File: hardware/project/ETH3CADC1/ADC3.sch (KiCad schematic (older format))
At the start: 45 parts, among them U801 DG211B, U802 OPA2192, U803 DG419xY, U804 LT5400-100k-100k, U805 LT5400-5k-1k, U806 OPA177, U807 OPA140, U808 OPA192, U809 LT5400-10k-10k, U810 LM311

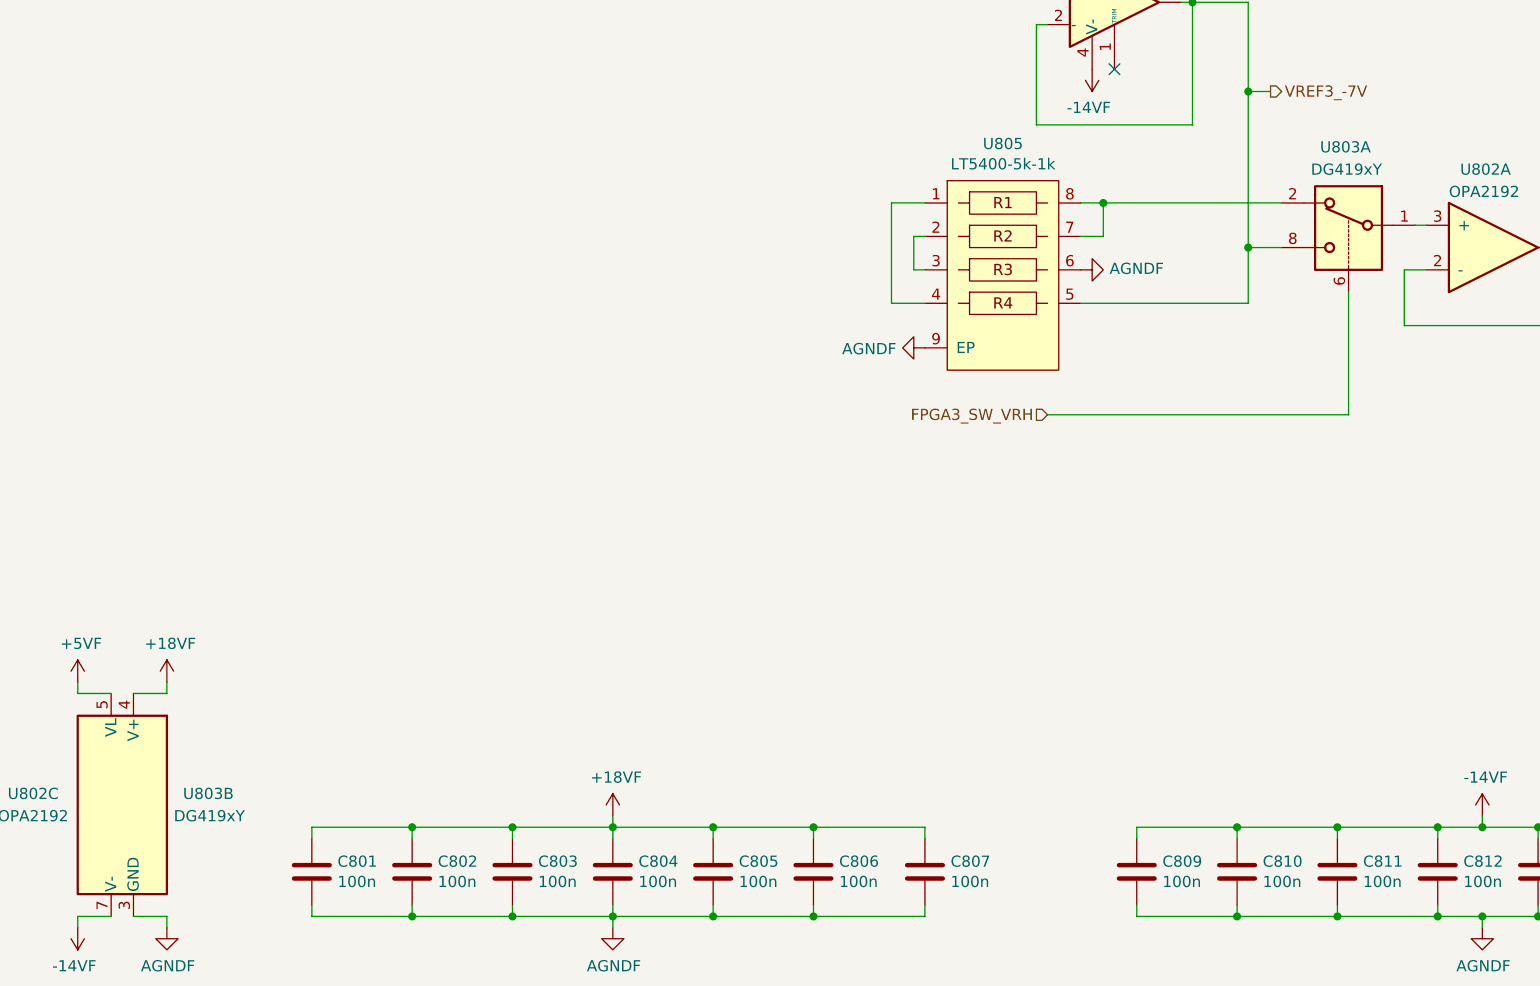
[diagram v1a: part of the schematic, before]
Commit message: Fixed mistake with DG419. Never use DG419Lxx variant.
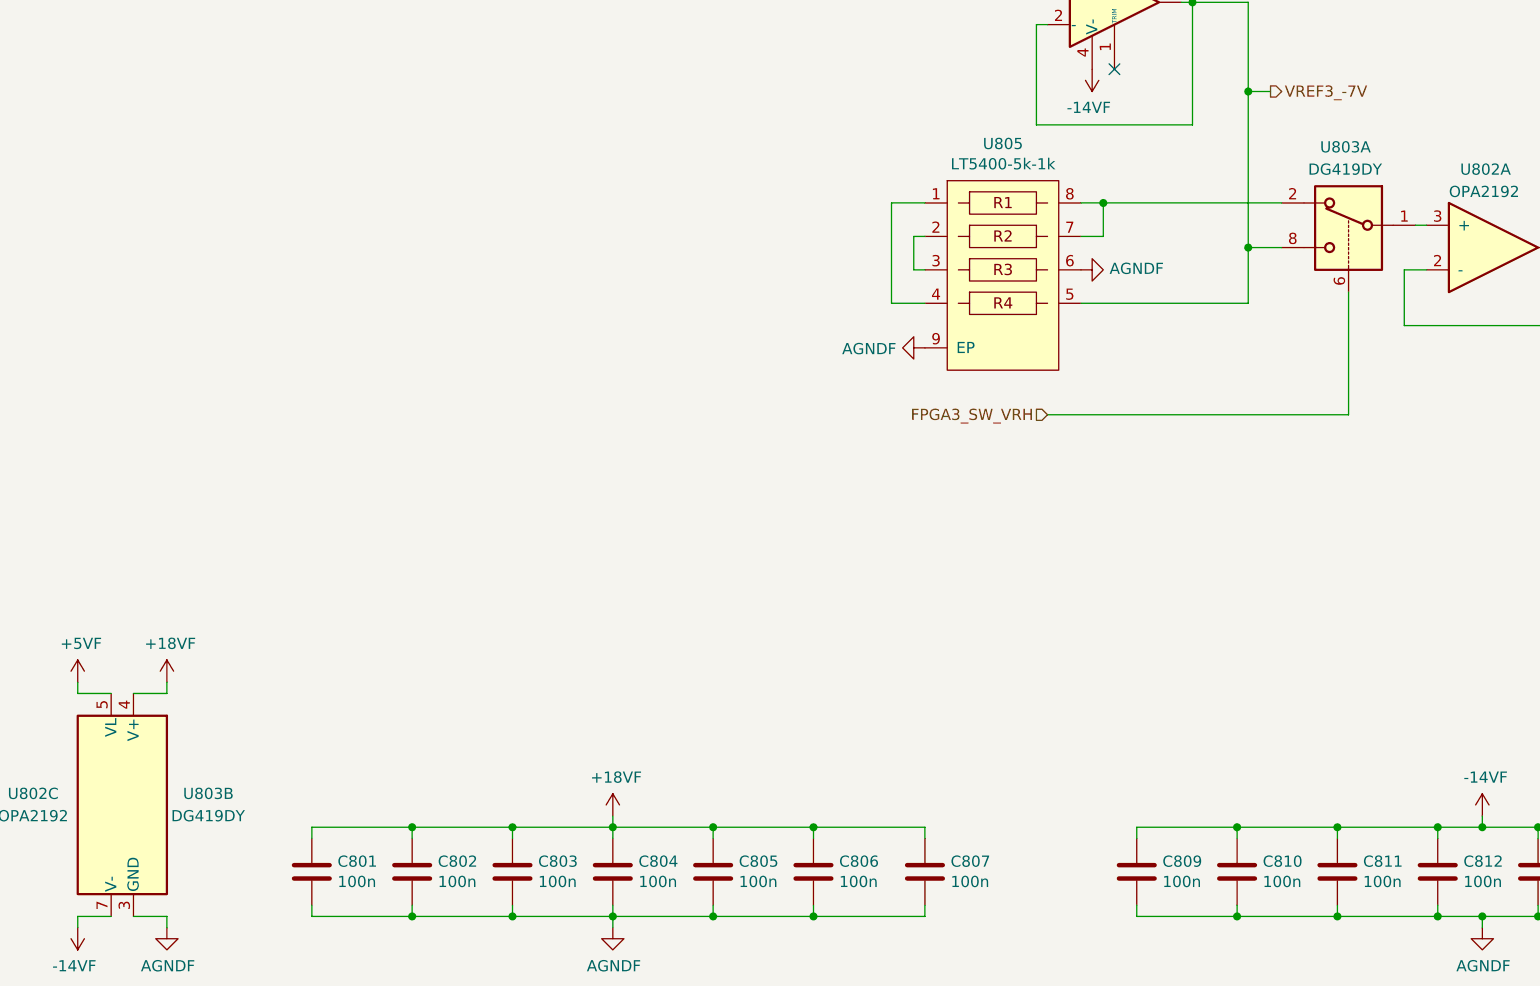
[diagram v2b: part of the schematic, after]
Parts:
- U803: value DG419xY -> DG419DY
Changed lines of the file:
@@
 AR Path="/605B3009/605E7BBD" Ref="U803"  Part="1"
 F 0 "U803" H 7950 7850 50  0000 L CNN
-F 1 "DG419xY" H 7900 7750 50  0000 L CNN
+F 1 "DG419DY" H 7900 7750 50  0000 L CNN
 F 2 "Package_SO:SOIC-8_3.9x4.9mm_P1.27mm" H 8050 7300 50  0001 C CNN
 F 3 "https://datasheets.maximintegrated.com/en/ds/DG417-DG419.pdf" H 8050 7600 50  0001 C CNN
@@
 AR Path="/605B3009/605E7C4B" Ref="U803"  Part="2"
 F 0 "U803" H 2150 10350 50  0000 L CNN
-F 1 "DG419xY" H 2100 10250 50  0000 L CNN
+F 1 "DG419DY" H 2100 10250 50  0000 L CNN
 F 2 "Package_SO:SOIC-8_3.9x4.9mm_P1.27mm" H 2600 10000 50  0001 C CNN
 F 3 "https://datasheets.maximintegrated.com/en/ds/DG417-DG419.pdf" H 2600 10300 50  0001 C CNN

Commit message: Development
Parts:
- removed C801, C802, C803, C804, C805, C806, C807, C809, C810, C811, C812, C814, C816, C817, C818, C819, C820, C821: 100n, Capacitor_SMD:C_0402_1005Metric_Pad0.74x0.62mm_HandSolder, symbol Device:C
- removed C808: 2n2/SMD, Capacitor_SMD:C_0603_1608Metric_Pad1.08x0.95mm_HandSolder, symbol Device:C
- removed C813: 33p, Capacitor_SMD:C_0402_1005Metric_Pad0.74x0.62mm_HandSolder, symbol Device:C
- removed C815: DNP, Capacitor_SMD:C_0402_1005Metric_Pad0.74x0.62mm_HandSolder, symbol Device:C
- removed D801, D802: BAV21W, Diode_SMD:D_SOD-123, symbol Device:D
- removed R801, R802, R804, R805, R809: 10, Resistor_SMD:R_0402_1005Metric_Pad0.72x0.64mm_HandSolder, symbol Device:R
- removed R803: 12k/.05%, Resistor_SMD:R_0603_1608Metric_Pad0.98x0.95mm_HandSolder, symbol Device:R
- removed R806: 62k, Resistor_SMD:R_0402_1005Metric_Pad0.72x0.64mm_HandSolder, symbol Device:R
- removed R807: 620/.05%, Resistor_SMD:R_0603_1608Metric_Pad0.98x0.95mm_HandSolder, symbol Device:R
- removed R808, R812: 3k9/.05%, Resistor_SMD:R_0603_1608Metric_Pad0.98x0.95mm_HandSolder, symbol Device:R
- removed R810: 62/.1%, Resistor_SMD:R_0603_1608Metric_Pad0.98x0.95mm_HandSolder, symbol Device:R
- removed R811: 39k/.05%, Resistor_SMD:R_0603_1608Metric_Pad0.98x0.95mm_HandSolder, symbol Device:R
- removed U801: DG211B, Package_SO:TSSOP-16_4.4x5mm_P0.65mm, symbol ETH3CDAQ1:DG211
- removed U802: OPA2192, Package_SO:SOIC-8_3.9x4.9mm_P1.27mm, symbol ETH3CDAQ1:OPA2192
- removed U803: DG419DY, Package_SO:SOIC-8_3.9x4.9mm_P1.27mm, symbol Analog_Switch:DG419xY
- removed U804: LT5400-100k-100k, Package_SO:MSOP-8-1EP_3x3mm_P0.65mm_EP1.73x1.85mm_ThermalVias, symbol ETH3CDAQ1:LT5400-100k-100k
- removed U805: LT5400-5k-1k, Package_SO:MSOP-8-1EP_3x3mm_P0.65mm_EP1.73x1.85mm_ThermalVias, symbol ETH3CDAQ1:LT5400-5k-1k
- removed U806: OPA177, Package_SO:SOIC-8_3.9x4.9mm_P1.27mm, symbol ETH3CDAQ1:OPA177
- removed U807: OPA140, Package_SO:SOIC-8_3.9x4.9mm_P1.27mm, symbol ETH3CDAQ1:OPA140
- removed U808: OPA192, Package_SO:SOIC-8_3.9x4.9mm_P1.27mm, symbol ETH3CDAQ1:OPA192
- removed U809: LT5400-10k-10k, Package_SO:MSOP-8-1EP_3x3mm_P0.65mm_EP1.73x1.85mm_ThermalVias, symbol ETH3CDAQ1:LT5400-10k-10k
- removed U810: LM311, Package_SO:SOIC-8_3.9x4.9mm_P1.27mm, symbol Comparator:LM311
- added C1701, C1702, C1703, C1704, C1705, C1706, C1707, C1708, C1709, C1711, C1712, C1713, C1714, C1715, C1717, C1718, C1719, C1720, C1721: 100n, Capacitor_SMD:C_0402_1005Metric_Pad0.74x0.62mm_HandSolder, symbol Device:C
- added C1710: 2n2/SMD, Capacitor_SMD:C_0603_1608Metric_Pad1.08x0.95mm_HandSolder, symbol Device:C
- added C1716: 33p, Capacitor_SMD:C_0402_1005Metric_Pad0.74x0.62mm_HandSolder, symbol Device:C
- added D1701, D1702: BAV21W, Diode_SMD:D_SOD-123, symbol Device:D
- added R1701, R1702, R1703, R1704, R1707: 10k, Resistor_SMD:R_0402_1005Metric_Pad0.72x0.64mm_HandSolder, symbol Device:R
- added R1705: 10M, Resistor_SMD:R_0603_1608Metric_Pad0.98x0.95mm_HandSolder, symbol Device:R
- added R1706: 0, Resistor_SMD:R_0402_1005Metric_Pad0.72x0.64mm_HandSolder, symbol Device:R
- added R1708, R1718: 62/.1%, Resistor_SMD:R_0603_1608Metric_Pad0.98x0.95mm_HandSolder, symbol Device:R
- added R1709, R1710, R1712, R1713, R1717: 10, Resistor_SMD:R_0402_1005Metric_Pad0.72x0.64mm_HandSolder, symbol Device:R
- added R1711: 12k/.05%, Resistor_SMD:R_0603_1608Metric_Pad0.98x0.95mm_HandSolder, symbol Device:R
- added R1714: 62k, Resistor_SMD:R_0402_1005Metric_Pad0.72x0.64mm_HandSolder, symbol Device:R
- added R1715: 620/.05%, Resistor_SMD:R_0603_1608Metric_Pad0.98x0.95mm_HandSolder, symbol Device:R
- added R1716, R1720: 3k9/.05%, Resistor_SMD:R_0603_1608Metric_Pad0.98x0.95mm_HandSolder, symbol Device:R
- added R1719: 39k/.05%, Resistor_SMD:R_0603_1608Metric_Pad0.98x0.95mm_HandSolder, symbol Device:R
- added U1701, U1703: DG211, Package_SO:TSSOP-16_4.4x5mm_P0.65mm, symbol ETH3CDAQ1:DG211
- added U1702: DG211B, Package_SO:TSSOP-16_4.4x5mm_P0.65mm, symbol ETH3CDAQ1:DG211
- added U1704: OPA2192, Package_SO:SOIC-8_3.9x4.9mm_P1.27mm, symbol ETH3CDAQ1:OPA2192
- added U1705: DG419DY, Package_SO:SOIC-8_3.9x4.9mm_P1.27mm, symbol Analog_Switch:DG419xY
- added U1706, U1710: OPA140, Package_SO:SOIC-8_3.9x4.9mm_P1.27mm, symbol ETH3CDAQ1:OPA140
- added U1707: LT5400-100k-100k, Package_SO:MSOP-8-1EP_3x3mm_P0.65mm_EP1.73x1.85mm_ThermalVias, symbol ETH3CDAQ1:LT5400-100k-100k
- added U1708: LT5400-5k-1k, Package_SO:MSOP-8-1EP_3x3mm_P0.65mm_EP1.73x1.85mm_ThermalVias, symbol ETH3CDAQ1:LT5400-5k-1k
- added U1709: OPA177, Package_SO:SOIC-8_3.9x4.9mm_P1.27mm, symbol ETH3CDAQ1:OPA177
- added U1711: LT5400-10k-10k, Package_SO:MSOP-8-1EP_3x3mm_P0.65mm_EP1.73x1.85mm_ThermalVias, symbol ETH3CDAQ1:LT5400-10k-10k
- added U1712: OPA192, Package_SO:SOIC-8_3.9x4.9mm_P1.27mm, symbol ETH3CDAQ1:OPA192
- added U1713: LM311, Package_SO:SOIC-8_3.9x4.9mm_P1.27mm, symbol Comparator:LM311
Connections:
- net +18VF: now also C1701.1, C1702.1, C1703.1, C1705.1, C1706.1, C1707.1, C1708.1, R1709.1, R1712.1, U1701.13 (V+), U1702.13 (V+), U1704.4 (V-), U1705.4 (V+), U1706.7 (V+), U1709.7 (V+)
- net -14VF: now also C1709.1, C1711.1, C1712.1, C1713.1, C1714.1, C1715.1, C1717.1, C1718.1, R1710.2, R1713.2, R1717.2, U1701.4 (V-), U1702.4 (V-), U1704.8 (V+), U1705.7 (V-), U1706.4 (V-), U1709.4 (V-)
- net ADIN3: now also R1701.2
- net AD_COMP3: now also R1720.2, U1713.7
- net AGNDF: now also C1701.2, C1702.2, C1703.2, C1704.2, C1705.2, C1706.2, C1707.2, C1708.2, C1709.2, C1711.2, C1712.2, C1713.2, C1714.2, C1715.2, C1717.2, C1718.2, R1702.2, R1705.2, R1715.2, U1701.5 (GND), U1702.5 (GND), U1704.6 (-), U1705.3 (GND), U1707.9 (EP), U1708.6, U1708.9 (EP), U1710.3 (+), U1711.9 (EP), U1712.3 (+)
- net DGNDF: now also C1719.2, C1720.2, U1713.1 (GND)
- net FGPA3_AD_ID: now also U1702.16
- net FGPA3_AD_IIN: now also U1702.1
- net FGPA3_AD_IRN: now also U1702.8
- net FGPA3_AD_IRP: now also U1702.9
- net FPGA3_SW_VRH: now also U1705.6
- net VREF+: now also U1704.7, U1707.4, U1711.1, U1711.2
- net VREF-: now also U1704.1, U1704.2 (-), U1707.3, U1711.3, U1711.4
- net VREF_N7V_LPF: now also R1704.2, R1708.2
- new net: U1707.1, U1707.2
- new net: U1702.6, U1707.5
- new net: U1702.11, U1707.6
- new net: U1702.2, U1707.7
- new net: R1707.1, U1707.8
- new net: C1710.2, U1702.10, U1702.14, U1702.3, U1702.7, U1710.2 (-)
- new net: U1704.5 (+), U1711.5, U1711.6, U1711.7, U1711.8
- new net: C1710.1, R1711.2, U1702.15, U1710.6
- new net: U1704.3 (+), U1705.1
- new net: U1705.2, U1708.7, U1708.8
- new net: U1705.8, U1708.5, U1709.2 (-), U1709.6
- new net: R1706.1, R1707.2, U1706.2 (-), U1706.6
- new net: R1705.1, R1706.2, U1703.10, U1703.15, U1703.3, U1703.6, U1706.3 (+)
- new net: C1716.2, D1701.2 (A), D1702.1 (K), R1711.1, R1714.2, U1712.2 (-)
- new net: R1713.1, U1712.4 (V-)
- new net: C1716.1, D1701.1 (K), D1702.2 (A), R1714.1, R1716.2, U1712.6
- new net: R1712.2, U1712.7 (V+)
- new net: R1704.1, U1703.14
- new net: R1703.1, U1703.11
- new net: C1704.1, R1708.1, U1709.3 (+)
- new net: R1702.1, U1703.7
- new net: R1710.1, U1710.4 (V-)
- new net: U1708.1, U1708.4
- new net: U1708.2, U1708.3
- new net: R1701.1, U1703.2
- new net: R1709.2, U1710.7 (V+)
- new net: R1716.1, U1713.2 (+)
- new net: R1715.1, U1713.3 (-)
- new net: C1721.2, R1717.1, U1713.4 (V-)
- new net: R1719.2, U1713.5 (BAL)
- new net: R1718.2, R1719.1, R1720.1
- new net +10VRF: R1703.2
- new net +3.3VF: C1719.1, C1720.1, C1721.1, R1718.1, U1701.12 (VL), U1702.12 (VL), U1705.5 (VL), U1713.8 (V+)
- new net FPGA3_MUX_ADIN: U1703.1
- new net FPGA3_MUX_GND: U1703.8
- new net FPGA3_MUX_N7V: U1703.16
- new net FPGA3_MUX_P10V: U1703.9
- no-connect marks 3 -> 5

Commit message: PCB layout
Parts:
- renumbered U1703 to U1701, U1704 to U1703, U1705 to U1704, U1706 to U1705, U1707 to U1706, U1708 to U1707, U1709 to U1708, U1710 to U1709, U1711 to U1710, U1712 to U1711, U1713 to U1712
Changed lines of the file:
@@
 AR Path="/5FCCC067/5E45E5A5" Ref="U?"  Part="2"
 AR Path="/5FD74AB8/5E45E5A5" Ref="U?"  Part="3"
-AR Path="/60441CDA/5E45E5A5" Ref="U1704"  Part="3"
-F 0 "U1704" H 2950 10300 50  0000 C CNN
+AR Path="/60441CDA/5E45E5A5" Ref="U1703"  Part="3"
+F 0 "U1703" H 2950 10300 50  0000 C CNN
 F 1 "OPA2192" H 2950 10400 50  0000 C CNN
 F 2 "Package_SO:SOIC-8_3.9x4.9mm_P1.27mm" H 2650 10550 50  0001 C CNN
@@
 $EndComp
 $Comp
-L Analog_Switch:DG419xY U1705
+L Analog_Switch:DG419xY U1704
 U 2 1 60504215
 P 3400 10350
-F 0 "U1705" H 2950 10400 50  0000 L CNN
+F 0 "U1704" H 2950 10400 50  0000 L CNN
 F 1 "DG419DY" H 2900 10300 50  0000 L CNN
 F 2 "Package_SO:SOIC-8_3.9x4.9mm_P1.27mm" H 3400 10050 50  0001 C CNN
@@
 	7400 4100 7300 4100
 $Comp
-L ETH3CDAQ1:OPA192 U1712
+L ETH3CDAQ1:OPA192 U1711
 U 1 1 5FECE3D3
 P 9750 2850
-F 0 "U1712" H 9900 3100 50  0000 L CNN
+F 0 "U1711" H 9900 3100 50  0000 L CNN
 F 1 "OPA192" H 9800 3000 50  0000 L CNN
 F 2 "Package_SO:SOIC-8_3.9x4.9mm_P1.27mm" H 9800 2900 50  0001 C CNN
@@
 AR Path="/5FCCC067/60504252" Ref="U?"  Part="1"
 AR Path="/5FD74AB8/60504252" Ref="U?"  Part="1"
-AR Path="/60441CDA/60504252" Ref="U1710"  Part="1"
-F 0 "U1710" H 8350 3200 50  0000 L CNN
+AR Path="/60441CDA/60504252" Ref="U1709"  Part="1"
+F 0 "U1709" H 8350 3200 50  0000 L CNN
 F 1 "OPA140" H 8300 3100 50  0000 L CNN
 F 2 "Package_SO:SOIC-8_3.9x4.9mm_P1.27mm" H 8250 3000 50  0001 C CNN
@@
 AR Path="/5FCCC067/60504272" Ref="U?"  Part="1"
 AR Path="/5FD74AB8/60504272" Ref="U?"  Part="1"
-AR Path="/60441CDA/60504272" Ref="U1713"  Part="1"
-F 0 "U1713" H 11800 3200 50  0000 L CNN
+AR Path="/60441CDA/60504272" Ref="U1712"  Part="1"
+F 0 "U1712" H 11800 3200 50  0000 L CNN
 F 1 "LM311" H 11800 3100 50  0000 L CNN
 F 2 "Package_SO:SOIC-8_3.9x4.9mm_P1.27mm" H 11600 2950 50  0001 C CNN
@@
 AR Path="/5FCCC067/5E3943C8" Ref="U?"  Part="1"
 AR Path="/5FD74AB8/5E3943C8" Ref="U?"  Part="1"
-AR Path="/60441CDA/5E3943C8" Ref="U1707"  Part="1"
-F 0 "U1707" H 5150 2700 50  0000 C CNN
+AR Path="/60441CDA/5E3943C8" Ref="U1706"  Part="1"
+F 0 "U1706" H 5150 2700 50  0000 C CNN
 F 1 "LT5400-100k-100k" H 5150 2600 50  0000 C CNN
 F 2 "Package_SO:MSOP-8-1EP_3x3mm_P0.65mm_EP1.73x1.85mm_ThermalVias" H 5150 2150 50  0001 C CNN
@@
 AR Path="/5FCCC067/602EA97D" Ref="U?"  Part="1"
 AR Path="/5FD74AB8/602EA97D" Ref="U?"  Part="1"
-AR Path="/60441CDA/602EA97D" Ref="U1709"  Part="1"
-F 0 "U1709" H 6350 6600 50  0000 L CNN
+AR Path="/60441CDA/602EA97D" Ref="U1708"  Part="1"
+F 0 "U1708" H 6350 6600 50  0000 L CNN
 F 1 "OPA177" H 6300 6500 50  0000 L CNN
 F 2 "Package_SO:SOIC-8_3.9x4.9mm_P1.27mm" H 6250 6400 50  0001 C CNN
@@
 AR Path="/5FCCC067/60504216" Ref="U?"  Part="1"
 AR Path="/5FD74AB8/60504216" Ref="U?"  Part="1"
-AR Path="/60441CDA/60504216" Ref="U1708"  Part="1"
-F 0 "U1708" H 5700 8115 50  0000 C CNN
+AR Path="/60441CDA/60504216" Ref="U1707"  Part="1"
+F 0 "U1707" H 5700 8115 50  0000 C CNN
 F 1 "LT5400-5k-1k" H 5700 8024 50  0000 C CNN
 F 2 "Package_SO:MSOP-8-1EP_3x3mm_P0.65mm_EP1.73x1.85mm_ThermalVias" H 5700 7650 50  0001 C CNN
@@
 AR Path="/5FCCC067/5E3AB8F0" Ref="U?"  Part="1"
 AR Path="/5FD74AB8/5E3AB8F0" Ref="U?"  Part="1"
-AR Path="/60441CDA/5E3AB8F0" Ref="U1711"  Part="1"
-F 0 "U1711" H 9150 7865 50  0000 C CNN
+AR Path="/60441CDA/5E3AB8F0" Ref="U1710"  Part="1"
+F 0 "U1710" H 9150 7865 50  0000 C CNN
 F 1 "LT5400-10k-10k" H 9150 7774 50  0000 C CNN
 F 2 "Package_SO:MSOP-8-1EP_3x3mm_P0.65mm_EP1.73x1.85mm_ThermalVias" H 9150 7400 50  0001 C CNN
@@
 AR Path="/5FCCC067/5E45E095" Ref="U?"  Part="1"
 AR Path="/5FD74AB8/5E45E095" Ref="U?"  Part="2"
-AR Path="/60441CDA/5E45E095" Ref="U1704"  Part="2"
-F 0 "U1704" H 10050 7917 50  0000 C CNN
+AR Path="/60441CDA/5E45E095" Ref="U1703"  Part="2"
+F 0 "U1703" H 10050 7917 50  0000 C CNN
 F 1 "OPA2192" H 10050 7826 50  0000 C CNN
 F 2 "Package_SO:SOIC-8_3.9x4.9mm_P1.27mm" H 10000 7700 50  0001 C CNN
@@
 NoConn ~ 6200 6650
 $Comp
-L Analog_Switch:DG419xY U1705
+L Analog_Switch:DG419xY U1704
 U 1 1 5E5E2DE0
 P 7250 7250
-F 0 "U1705" H 7150 7500 50  0000 L CNN
+F 0 "U1704" H 7150 7500 50  0000 L CNN
 F 1 "DG419DY" H 7100 7400 50  0000 L CNN
 F 2 "Package_SO:SOIC-8_3.9x4.9mm_P1.27mm" H 7250 6950 50  0001 C CNN
@@
 AR Path="/5FCCC067/60504214" Ref="U?"  Part="3"
 AR Path="/5FD74AB8/60504214" Ref="U?"  Part="1"
-AR Path="/60441CDA/60504214" Ref="U1704"  Part="1"
-F 0 "U1704" H 7750 7800 50  0000 L CNN
+AR Path="/60441CDA/60504214" Ref="U1703"  Part="1"
+F 0 "U1703" H 7750 7800 50  0000 L CNN
 F 1 "OPA2192" H 7700 7700 50  0000 L CNN
 F 2 "Package_SO:SOIC-8_3.9x4.9mm_P1.27mm" H 7850 7600 50  0001 C CNN
@@
 	500  9100 16050 9100
 $Comp
-L ETH3CDAQ1:OPA140 U1706
+L ETH3CDAQ1:OPA140 U1705
 U 1 1 5FE103EF
 P 3850 1500
-F 0 "U1706" H 3900 1750 50  0000 L CNN
+F 0 "U1705" H 3900 1750 50  0000 L CNN
 F 1 "OPA140" H 3850 1650 50  0000 L CNN
 F 2 "Package_SO:SOIC-8_3.9x4.9mm_P1.27mm" H 3900 1550 50  0001 C CNN
@@
 $EndComp
 $Comp
-L ETH3CDAQ1:DG211 U1703
+L ETH3CDAQ1:DG211 U1701
 U 2 1 6009676C
 P 2150 3700
-F 0 "U1703" H 2150 3967 50  0000 C CNN
+F 0 "U1701" H 2150 3967 50  0000 C CNN
 F 1 "DG211" H 2150 3876 50  0000 C CNN
 F 2 "Package_SO:TSSOP-16_4.4x5mm_P0.65mm" H 2150 3600 50  0001 C CNN
@@
 $EndComp
 $Comp
-L ETH3CDAQ1:DG211 U1703
+L ETH3CDAQ1:DG211 U1701
 U 3 1 6009949F
 P 2150 2950
-F 0 "U1703" H 2150 3217 50  0000 C CNN
+F 0 "U1701" H 2150 3217 50  0000 C CNN
 F 1 "DG211" H 2150 3126 50  0000 C CNN
 F 2 "Package_SO:TSSOP-16_4.4x5mm_P0.65mm" H 2150 2850 50  0001 C CNN
@@
 $EndComp
 $Comp
-L ETH3CDAQ1:DG211 U1703
+L ETH3CDAQ1:DG211 U1701
 U 4 1 6050423A
 P 2150 2200
-F 0 "U1703" H 2150 2467 50  0000 C CNN
+F 0 "U1701" H 2150 2467 50  0000 C CNN
 F 1 "DG211" H 2150 2376 50  0000 C CNN
 F 2 "Package_SO:TSSOP-16_4.4x5mm_P0.65mm" H 2150 2100 50  0001 C CNN
@@
 $EndComp
 $Comp
-L ETH3CDAQ1:DG211 U1703
+L ETH3CDAQ1:DG211 U1701
 U 1 1 60504236
 P 2150 1400
-F 0 "U1703" H 2150 1667 50  0000 C CNN
+F 0 "U1701" H 2150 1667 50  0000 C CNN
 F 1 "DG211" H 2150 1576 50  0000 C CNN
 F 2 "Package_SO:TSSOP-16_4.4x5mm_P0.65mm" H 2150 1300 50  0001 C CNN
